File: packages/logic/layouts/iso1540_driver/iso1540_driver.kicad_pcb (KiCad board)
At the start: 2 copper layers, 3 parts

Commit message: Rebuild all
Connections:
- C1 pad 2: gnd-1 -> gnd
- C2 pad 2: gnd -> gnd-1
- U1 pad 2: line-3 -> line-2
- U1 pad 3: line -> line-1
- U1 pad 4: gnd -> gnd-1
- U1 pad 5: gnd-1 -> gnd
- U1 pad 6: line-2 -> line-3
- U1 pad 7: line-1 -> line
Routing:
- net (no net): track 0.00 -> 3.32 mm
- net hv-1: track 1.66 -> 0.00 mm
- net hv: track 1.66 -> 0.00 mm

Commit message: WIP update logic
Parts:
- C1, C2: footprint atopile:C0402-b3ef17 -> Samsung_Electro_Mechanics_CL05B104KO5NNNC:C0402
- U1: footprint atopile:SOIC-8_L4.9-W3.9-P1.27-LS6.0-BL-6ccfeb -> Texas_Instruments_ISO1540DR:SOIC-8_L4.9-W3.9-P1.27-LS6.0-BL
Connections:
- C1 pad 1: hv-1 -> hv
- C2 pad 1: hv -> hv-1
- U1 pad 1: hv -> hv-1
- U1 pad 2: line-2 -> line-1
- U1 pad 3: line-1 -> line-3
- U1 pad 6: line-3 -> line
- U1 pad 7: line -> line-2
- U1 pad 8: hv-1 -> hv

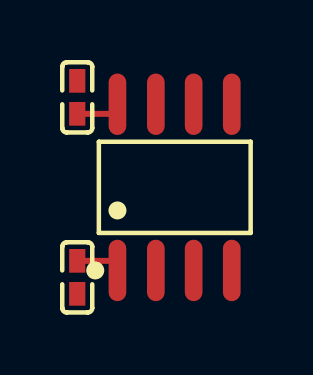
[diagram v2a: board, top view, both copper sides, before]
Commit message: Update 3D model locations
fix missing renders
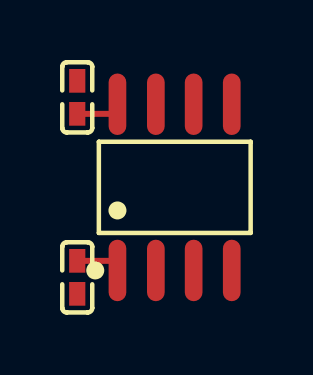
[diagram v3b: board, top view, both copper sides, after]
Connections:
- C1 pad 2: gnd -> gnd-1
- C2 pad 2: gnd-1 -> gnd
- U1 pad 2: line-1 -> line-3
- U1 pad 3: line-3 -> line-2
- U1 pad 4: gnd-1 -> gnd
- U1 pad 5: gnd -> gnd-1
- U1 pad 7: line-2 -> line-1
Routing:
- net (no net): track 3.32 -> 0.00 mm
- net hv-1: track 0.00 -> 1.66 mm
- net hv: track 0.00 -> 1.66 mm

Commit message: rebuild all packages & regenerate images of changed layouts (silk)
Add new scripts for version bump and build (based on atopile/packages)
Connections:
- C1 pad 2: gnd-1 -> gnd
- C2 pad 2: gnd -> gnd-1
- U1 pad 4: gnd -> gnd-1
- U1 pad 5: gnd-1 -> gnd
